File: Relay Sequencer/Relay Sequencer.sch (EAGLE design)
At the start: 51 parts, among them IC1 MEGA16-A, IC2 ULN2003AD, IC3 7805DT, IC4 74HC244DW, K1 351, K2 351, K3 351, K4 351

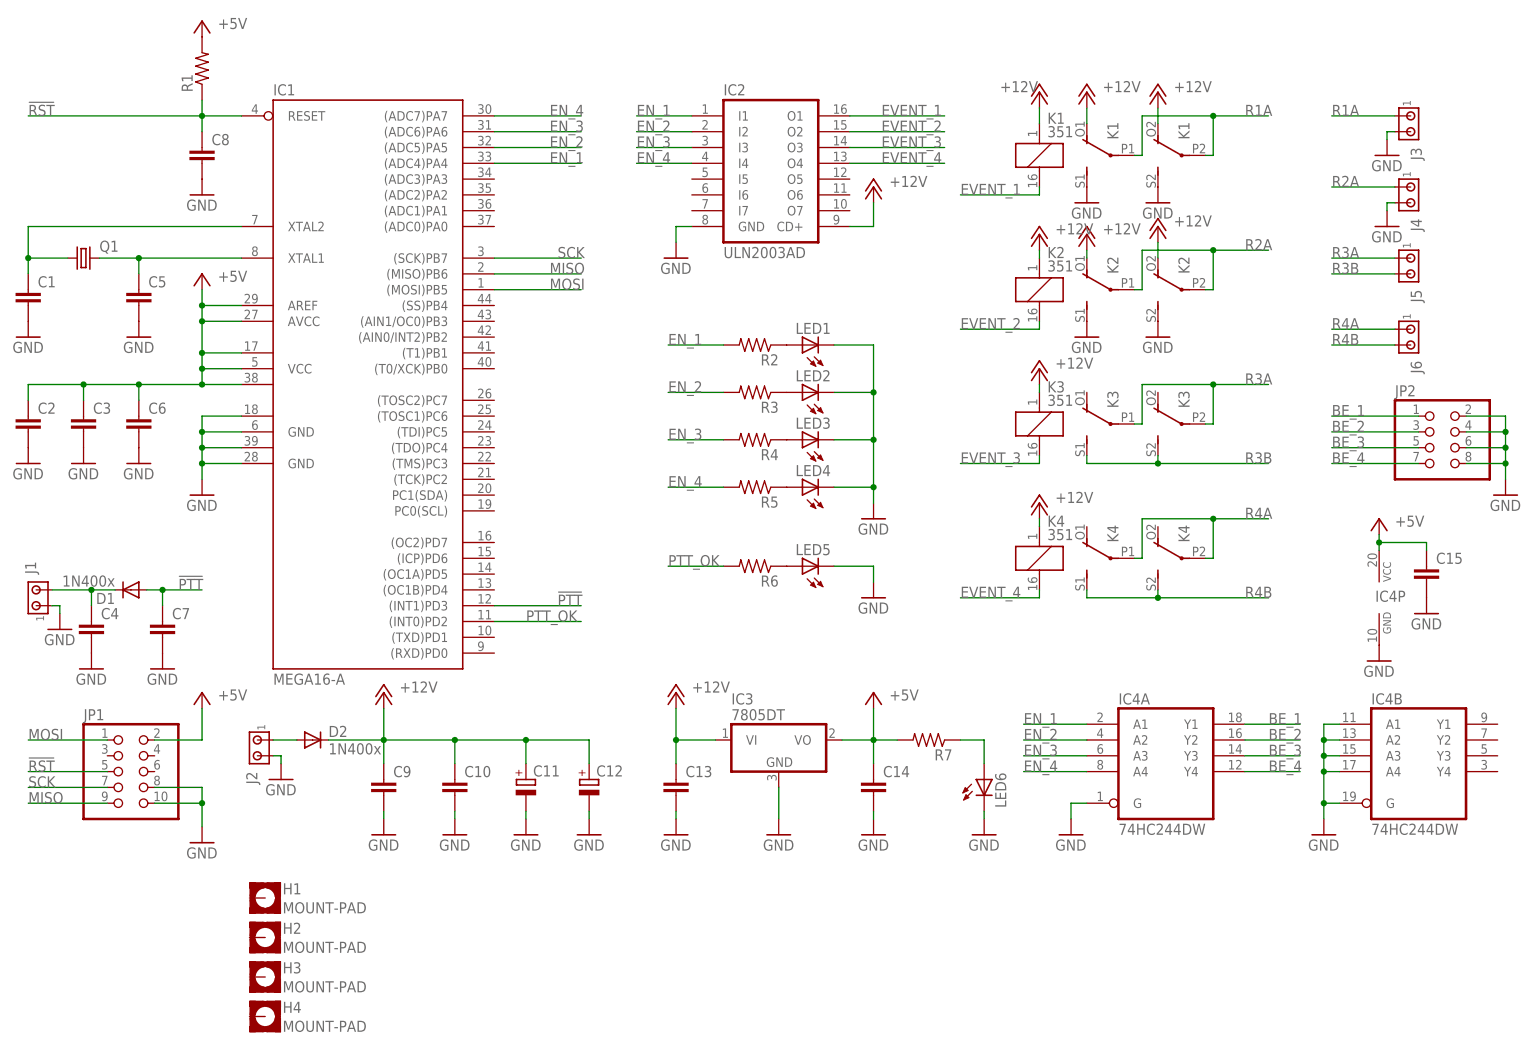
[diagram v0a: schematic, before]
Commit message: Revalue the components
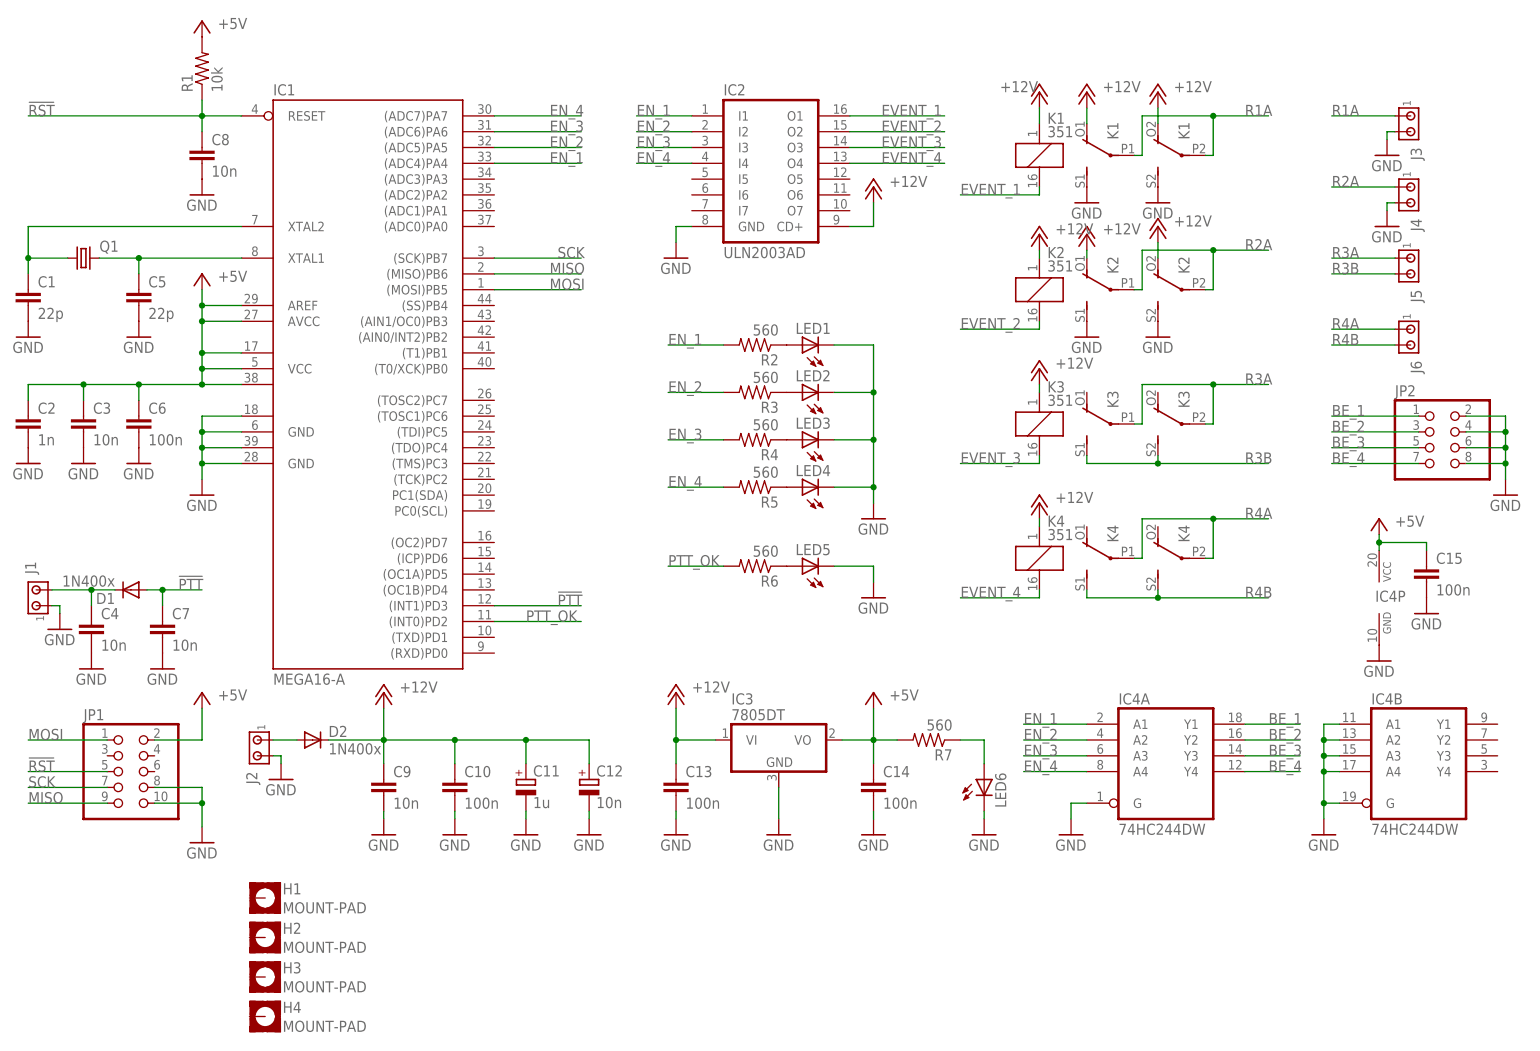
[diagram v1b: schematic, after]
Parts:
- C1, C5: value (none) -> 22p
- C10, C13, C14, C15, C6: value (none) -> 100n
- C11: value (none) -> 1u
- C12, C3, C4, C7, C8, C9: value (none) -> 10n
- C2: value (none) -> 1n
- R1: value (none) -> 10k
- R2, R3, R4, R5, R6, R7: value (none) -> 560
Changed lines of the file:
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@@
 <part name="IC2" library="uln-udn" deviceset="ULN2003A" device="D"/>
 <part name="Q1" library="crystal" deviceset="CRYSTAL" device="HC49S"/>
-<part name="C5" library="rcl" deviceset="C-EU" device="C1206"/>
-<part name="C1" library="rcl" deviceset="C-EU" device="C1206"/>
-<part name="R1" library="rcl" deviceset="R-US_" device="M1206"/>
+<part name="C5" library="rcl" deviceset="C-EU" device="C1206" value="22p"/>
+<part name="C1" library="rcl" deviceset="C-EU" device="C1206" value="22p"/>
+<part name="R1" library="rcl" deviceset="R-US_" device="M1206" value="10k"/>
 <part name="GND6" library="supply1" deviceset="GND" device=""/>
 <part name="GND1" library="supply1" deviceset="GND" device=""/>
 <part name="GND10" library="supply1" deviceset="GND" device=""/>
-<part name="C8" library="rcl" deviceset="C-EU" device="C1206"/>
+<part name="C8" library="rcl" deviceset="C-EU" device="C1206" value="10n"/>
 <part name="GND9" library="supply1" deviceset="GND" device=""/>
-<part name="C6" library="rcl" deviceset="C-EU" device="C1206"/>
+<part name="C6" library="rcl" deviceset="C-EU" device="C1206" value="100n"/>
 <part name="GND7" library="supply1" deviceset="GND" device=""/>
-<part name="C3" library="rcl" deviceset="C-EU" device="C1206"/>
+<part name="C3" library="rcl" deviceset="C-EU" device="C1206" value="10n"/>
 <part name="GND4" library="supply1" deviceset="GND" device=""/>
-<part name="C2" library="rcl" deviceset="C-EU" device="C1206"/>
+<part name="C2" library="rcl" deviceset="C-EU" device="C1206" value="1n"/>
 <part name="GND2" library="supply1" deviceset="GND" device=""/>
 <part name="GND14" library="supply1" deviceset="GND" device=""/>
 <part name="P+5" library="supply1" deviceset="+12V" device=""/>
-<part name="R4" library="rcl" deviceset="R-US_" device="M1206"/>
+<part name="R4" library="rcl" deviceset="R-US_" device="M1206" value="560"/>
 <part name="JP2" library="pinhead" deviceset="PINHD-2X4" device=""/>
 <part name="LED3" library="led" deviceset="LED" device="3MM"/>
-<part name="R5" library="rcl" deviceset="R-US_" device="M1206"/>
+<part name="R5" library="rcl" deviceset="R-US_" device="M1206" value="560"/>
 <part name="LED4" library="led" deviceset="LED" device="3MM"/>
-<part name="R2" library="rcl" deviceset="R-US_" device="M1206"/>
+<part name="R2" library="rcl" deviceset="R-US_" device="M1206" value="560"/>
 <part name="LED1" library="led" deviceset="LED" device="3MM"/>
-<part name="R3" library="rcl" deviceset="R-US_" device="M1206"/>
+<part name="R3" library="rcl" deviceset="R-US_" device="M1206" value="560"/>
 <part name="LED2" library="led" deviceset="LED" device="3MM"/>
 <part name="GND17" library="supply1" deviceset="GND" device=""/>
@@
 <part name="P+3" library="supply1" deviceset="+5V" device=""/>
 <part name="GND11" library="supply1" deviceset="GND" device=""/>
-<part name="R6" library="rcl" deviceset="R-US_" device="M1206"/>
+<part name="R6" library="rcl" deviceset="R-US_" device="M1206" value="560"/>
 <part name="LED5" library="led" deviceset="LED" device="3MM"/>
 <part name="GND18" library="supply1" deviceset="GND" device=""/>
@@
 <part name="D2" library="diode" deviceset="1N4148" device="DO35-10" value="1N400x"/>
 <part name="GND12" library="supply1" deviceset="GND" device=""/>
-<part name="C9" library="rcl" deviceset="C-EU" device="C1206"/>
-<part name="C10" library="rcl" deviceset="C-EU" device="C1206"/>
+<part name="C9" library="rcl" deviceset="C-EU" device="C1206" value="10n"/>
+<part name="C10" library="rcl" deviceset="C-EU" device="C1206" value="100n"/>
 <part name="GND13" library="supply1" deviceset="GND" device=""/>
 <part name="GND15" library="supply1" deviceset="GND" device=""/>
 <part name="GND16" library="supply1" deviceset="GND" device=""/>
-<part name="C11" library="rcl" deviceset="CPOL-EU" device="E5-8.5"/>
-<part name="C12" library="rcl" deviceset="CPOL-EU" device="E5-13"/>
+<part name="C11" library="rcl" deviceset="CPOL-EU" device="E5-8.5" value="1u"/>
+<part name="C12" library="rcl" deviceset="CPOL-EU" device="E5-13" value="10n"/>
 <part name="GND19" library="supply1" deviceset="GND" device=""/>
 <part name="P+4" library="supply1" deviceset="+12V" device=""/>
 <part name="IC3" library="linear" deviceset="78*" device="DT" technology="05"/>
-<part name="C13" library="rcl" deviceset="C-EU" device="C1206"/>
-<part name="C14" library="rcl" deviceset="C-EU" device="C1206"/>
+<part name="C13" library="rcl" deviceset="C-EU" device="C1206" value="100n"/>
+<part name="C14" library="rcl" deviceset="C-EU" device="C1206" value="100n"/>
 <part name="GND20" library="supply1" deviceset="GND" device=""/>
 <part name="GND21" library="supply1" deviceset="GND" device=""/>
@@
 <part name="P+6" library="supply1" deviceset="+12V" device=""/>
 <part name="P+11" library="supply1" deviceset="+5V" device=""/>
-<part name="R7" library="rcl" deviceset="R-US_" device="M1206"/>
+<part name="R7" library="rcl" deviceset="R-US_" device="M1206" value="560"/>
 <part name="LED6" library="led" deviceset="LED" device="3MM"/>
 <part name="GND23" library="supply1" deviceset="GND" device=""/>
@@
 <part name="FRAME1" library="frames" deviceset="A4L-LOC" device=""/>
 <part name="J2" library="con-amp" deviceset="MTA02-156" device=""/>
-<part name="C4" library="rcl" deviceset="C-EU" device="C1206"/>
-<part name="C7" library="rcl" deviceset="C-EU" device="C1206"/>
+<part name="C4" library="rcl" deviceset="C-EU" device="C1206" value="10n"/>
+<part name="C7" library="rcl" deviceset="C-EU" device="C1206" value="10n"/>
 <part name="GND5" library="supply1" deviceset="GND" device=""/>
 <part name="GND8" library="supply1" deviceset="GND" device=""/>
@@
 <part name="P+12" library="supply1" deviceset="+5V" device=""/>
 <part name="GND28" library="supply1" deviceset="GND" device=""/>
-<part name="C15" library="rcl" deviceset="C-EU" device="C1206"/>
+<part name="C15" library="rcl" deviceset="C-EU" device="C1206" value="100n"/>
 <part name="GND29" library="supply1" deviceset="GND" device=""/>
 <part name="GND24" library="supply1" deviceset="GND" device=""/>
